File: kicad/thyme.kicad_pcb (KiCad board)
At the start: 2 copper layers, 281.8 x 83.1 mm, 90 parts, among them P1 JST BATTERY L, P2 JST BATTERY R, SW1 SW_Push, SW10 SW_Push, SW11 SW_Push, SW12 SW_Push, SW13 SW_Push, SW14 SW_Push, SW15 SW_Push, SW16 SW_Push, SW17 SW_Push, SW18 SW_Push, SW19 SW_Push, SW2 SW_Push, SW20 SW_Push, SW21 SW_Push, SW22 SW_Push, SW23 SW_Push, SW24 SW_Push, SW25 SW_Push, SW26 SW_Push, SW27 SW_Push, SW28 SW_Push, SW29 SW_Push, SW3 SW_Push, SW30 SW_Push, SW31 SW_Push, SW32 SW_Push, SW33 SW_Push, SW34 SW_Push, SW35 SW_Push, SW36 SW_Push, SW37 SW_Push, SW38 SW_Push, SW39 SW_Push, SW4 SW_Push, SW40 SW_Push, SW41 SW_Push, SW42 SW_Push, SW44 SW_SPDT, SW45 SW_SPDT, SW5 SW_Push, SW6 SW_Push, SW7 SW_Push, SW8 SW_Push, SW9 SW_Push, U1 nice_nano, U2 nice_nano

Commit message: feat: add images
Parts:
- moved D28 30.2 mm to (256.4, 64.3)
- moved SW10 30.2 mm to (101.6, 58.2)
- moved SW13 30.2 mm to (120.6, 60.6)
- moved SW7 30.2 mm to (82.6, 63.0)
- moved D1 30.2 mm to (54.1, 68.7)
- moved D10 30.2 mm to (111.1, 62.1)
- moved D11 30.2 mm to (111.1, 81.1)
- moved D12 30.2 mm to (111.1, 100.1)
- moved D2 30.2 mm to (54.1, 88.2)
- moved D3 30.2 mm to (54.1, 107.2)
- moved D38 30.2 mm to (144.6, 118.9)
- moved D39 30.2 mm to (122.3, 121.4)
- moved D4 30.2 mm to (73.1, 69.2)
- moved D5 30.2 mm to (73.1, 88.2)
- moved D6 30.2 mm to (73.1, 107.2)
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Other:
- outline, holes or cut-outs redrawn

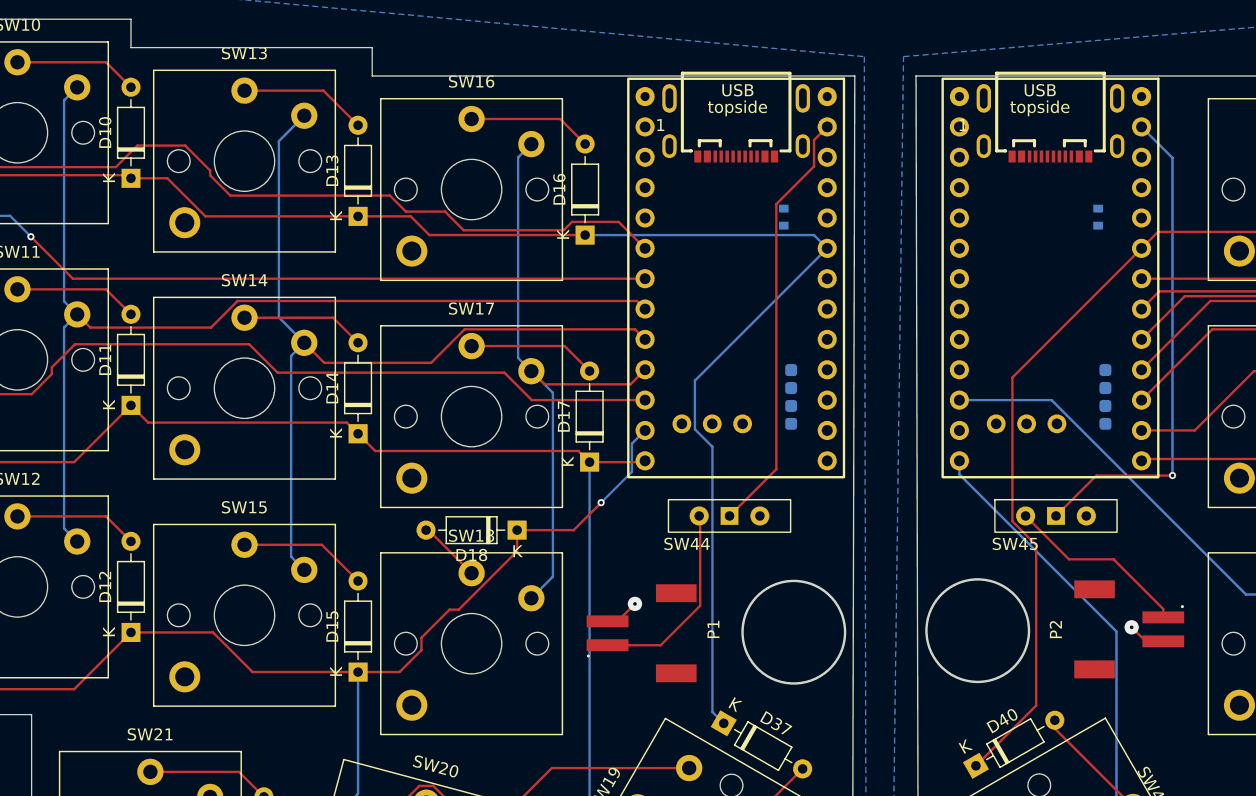
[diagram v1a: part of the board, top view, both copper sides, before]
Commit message: feat: move jst to top for machine pins
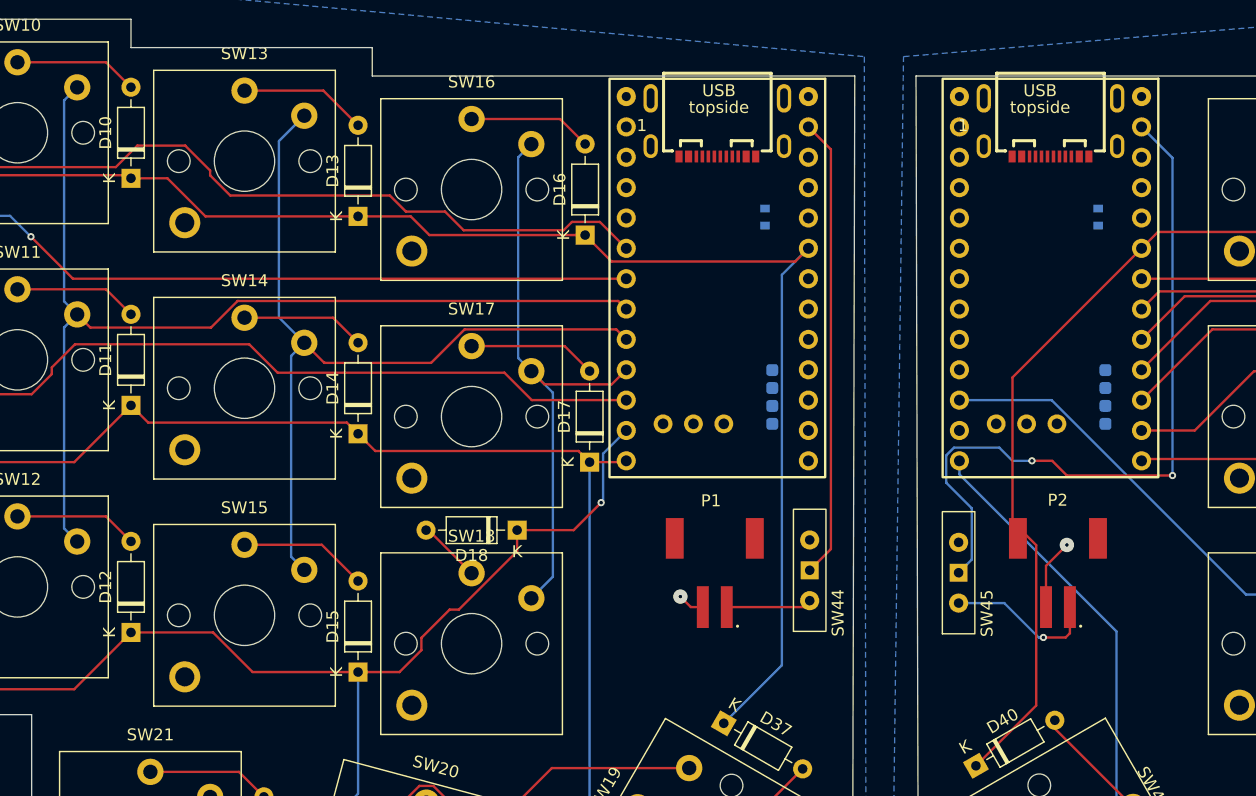
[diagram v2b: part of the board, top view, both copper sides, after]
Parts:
- moved SW45 9.43 mm to (180.4, 95.1), turned to 90 degrees
- moved P1 9.24 mm to (160.0, 97.9), turned to 0 degrees
- moved P2 9.01 mm to (188.7, 97.9), turned to 0 degrees
- moved SW44 8.10 mm to (167.9, 94.9), turned to 90 degrees
- moved U1 1.57 mm to (152.6, 55.2)
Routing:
- net Net-(SW45-B): track 41.4 -> 61.6 mm, vias 1 -> 2
- net LBATTERY_POSITIVE: track 16.7 -> 7.16 mm
- net L-ROW0: track 169.3 -> 166.0 mm
- net RPOWER-GND: track 3.13 -> 5.92 mm
- net Net-(SW44-B): track 35.9 -> 38.6 mm
- net RBATTERY_POSITIVE: track 15.5 -> 12.8 mm, vias 0 -> 1
- net L-COL5: track 50.9 -> 49.3 mm
- net L-ROW1: track 140.8 -> 139.2 mm
- net L-COL4: track 71.4 -> 69.8 mm
- net L-COL3: track 89.0 -> 87.4 mm
- net L-COL2: track 111.1 -> 109.6 mm
- net L-COL1: track 130.1 -> 128.6 mm
- net L-COL0: track 152.0 -> 150.5 mm
- net LPOWER-GND: track 2.90 -> 2.24 mm
- net L-ROW2: track 137.5 -> 136.9 mm
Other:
- outline, holes or cut-outs redrawn

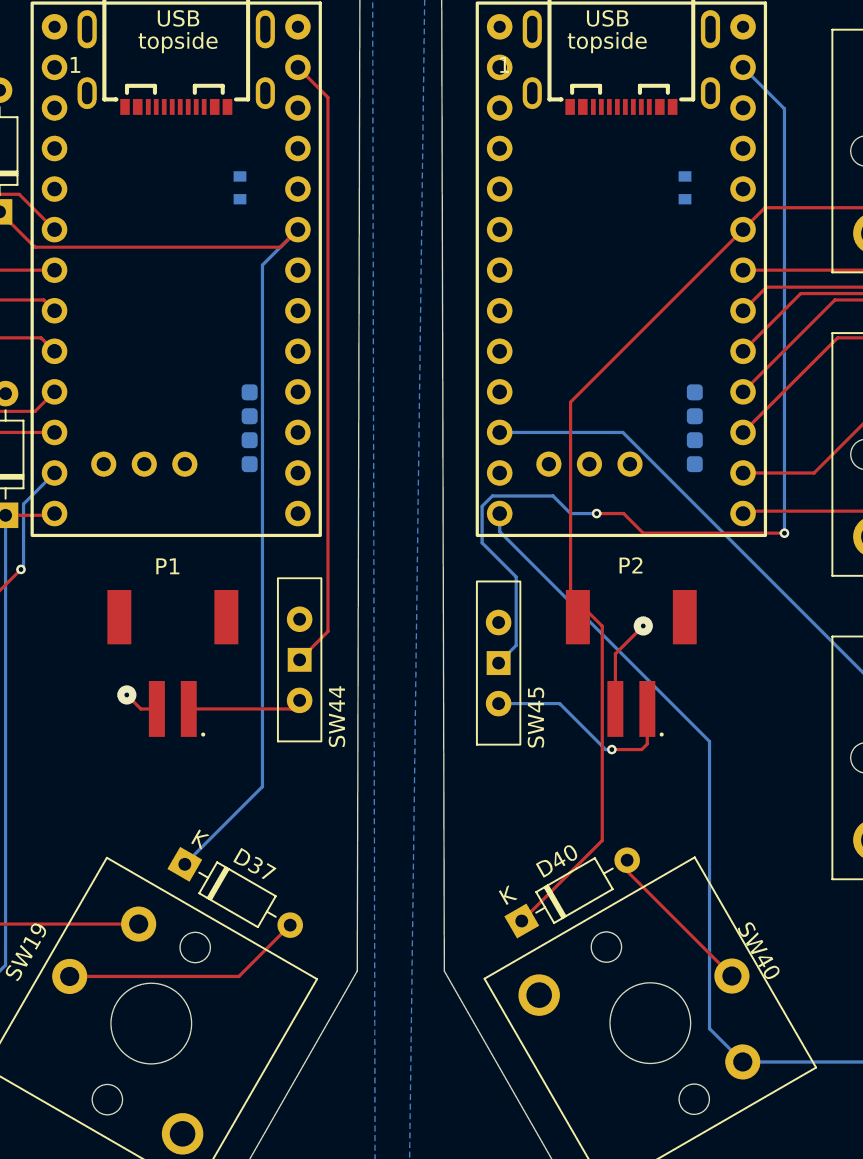
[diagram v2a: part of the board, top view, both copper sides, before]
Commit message: feat: move to jst tht connector and new switches
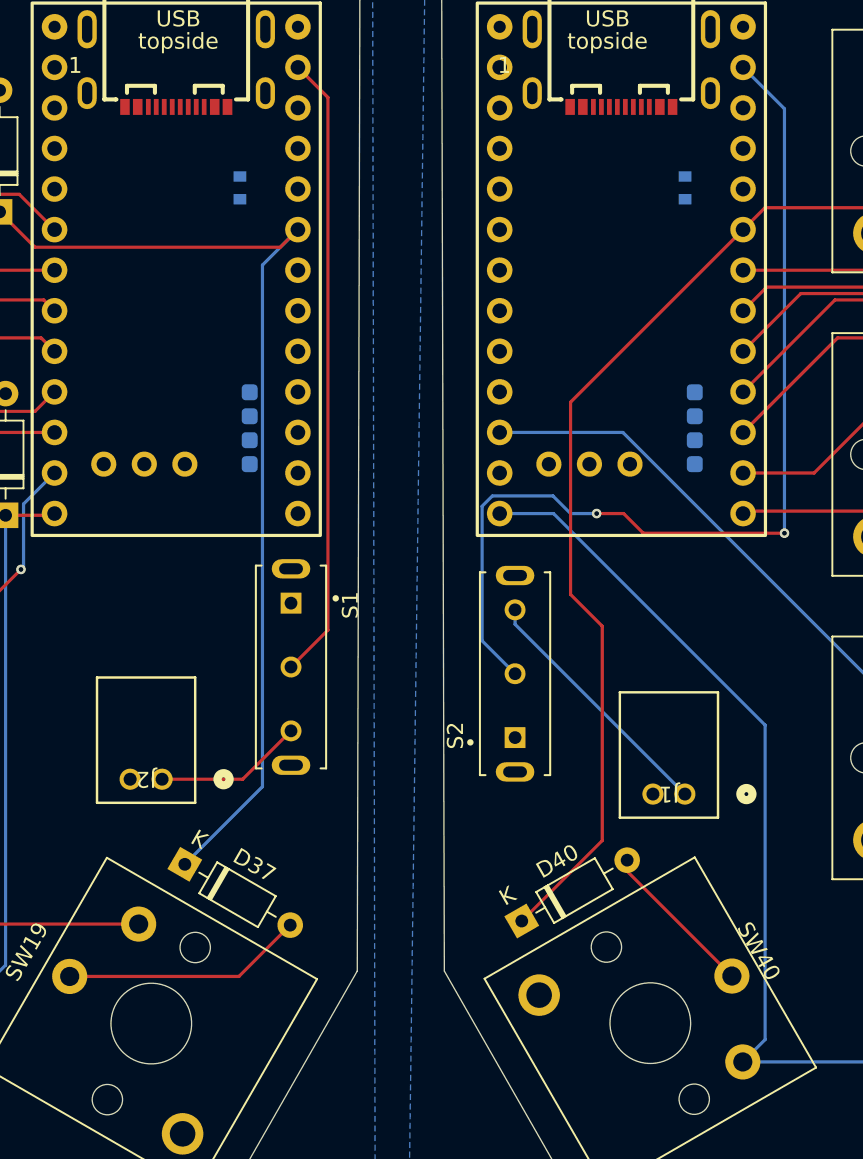
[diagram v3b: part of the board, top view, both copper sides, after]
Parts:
- removed P1: JST BATTERY L, libraries:JST_S2B-PH-SM4-TB
- removed P2: JST BATTERY R, libraries:JST_S2B-PH-SM4-TB
- removed SW44, SW45: SW_SPDT, Button_Switch_THT:SW_Slide-03_Wuerth-WS-SLTV_10x2.5x6.4_P2.54mm
- added J1: JST BATTERY R, libraries:CONN_S2B-PH-K-S_JST, F.Cu at (192.0, 103.3)
- added J2: JST BATTERY R, libraries:CONN_S2B-PH-K-S_JST, F.Cu at (159.3, 102.3)
- added S1: Power Switch, libraries:SW_SLW-1277744-3A-N-D, F.Cu at (167.4, 95.3)
- added S2: Power Switch, libraries:SW_SLW-1277744-3A-N-D, F.Cu at (181.4, 95.7)
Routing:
- net RPOWER-GND: track 5.92 -> 0.00 mm, vias 1 -> 0
- net R-COL6: track 87.4 -> 90.6 mm
- net RBATTERY_POSITIVE: track 12.8 -> 15.9 mm, vias 1 -> 0
- net LPOWER-GND: track 2.24 -> 0.00 mm, vias 1 -> 0
- net LBATTERY_POSITIVE: track 7.16 -> 9.33 mm
- net Net-(S1-Pad2): track 38.6 -> 39.3 mm
